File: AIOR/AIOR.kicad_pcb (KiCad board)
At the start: 2 copper layers, 85 x 56.5 mm, 158 parts, among them J20 Conn_01x04, J30 Conn_01x02, J31 Conn_01x02, J50 Conn_01x02, J70 Conn_01x01, J81 Conn_01x06, J82 5V 12V, J90 Conn_01x03, P1 CONN_02X20, P2 CONN_01X02, P3 CAN, P50 XPN, P60 SLX, P70 LCN, P8 Conn_01x02, P9 Conn_01x04, Q30 BTN8982TA, Q31 BTN8982TA, Q60 BC817, Q70 BC817, Q90 BC857, Q91 BC857, U1 MCP2517FD, U2 ISO1050, U20 L7833, U21 L7805, U22 DSPIC33EP128GM604, U23 Si8605, U24 MCP2562, U4 P82B715, U40 C8051F502, U41 ADUM1251, U42 MCP2561, U50 MAX3072E, U70 LM393, U81 L7805, U82 SI8641-SOIC, U83 4504, U90 SAA6579, Y1 4MHz, Y20 8MHz, Y90 4MHz

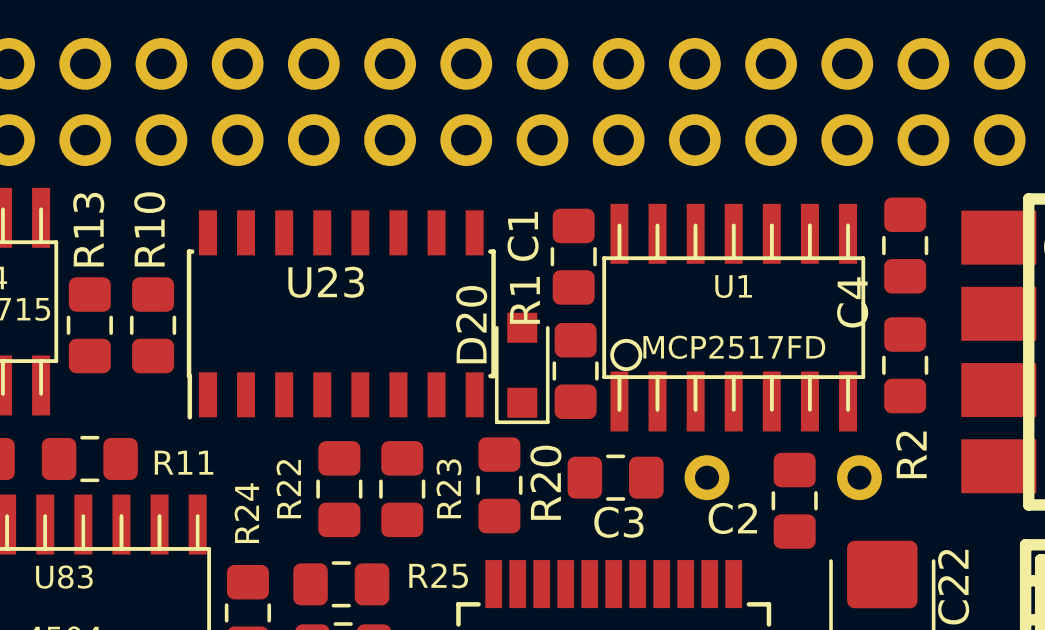
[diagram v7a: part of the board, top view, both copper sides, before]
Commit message: change some footprints
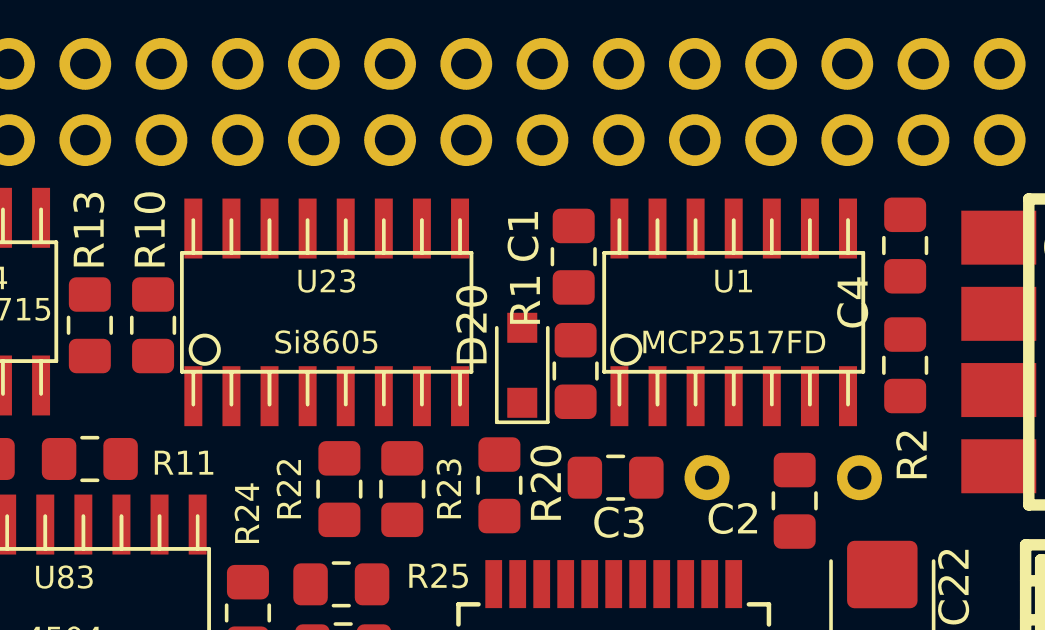
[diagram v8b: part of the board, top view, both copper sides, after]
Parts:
- U23: footprint Package_SO:SOIC-16_3.9x9.9mm_P1.27mm -> w_smd_dil:so-16
- moved U23 0.49 mm to (149.5, 82.5), turned to 0 degrees
- moved U1 0.18 mm to (163.1, 82.5)
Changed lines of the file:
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@@
-(kicad_pcb (version 20171130) (host pcbnew 5.1.2-f72e74a~84~ubuntu18.04.1)
+(kicad_pcb (version 20171130) (host pcbnew "(5.1.2-1)-1")
   (general
     (thickness 1.6)
@@
     (add_net "Net-(U1-Pad3)")
   )
+  (module w_smd_dil:so-16 (layer F.Cu)
+    (at 149.5 82.5)
+    (descr SO-16)
+    (fp_text reference U23 (at 0 -1.016) (layer F.SilkS)
+      (effects (font (size 0.7493 0.7493) (thickness 0.14986)))
+    )
+    (fp_text value Si8605 (at 0 1.016) (layer F.SilkS)
+      (effects (font (size 0.7493 0.7493) (thickness 0.14986)))
+    )
+    (fp_line (start 4.826 -1.9812) (end -4.826 -1.9812) (layer F.SilkS) (width 0.127))
+    (fp_line (start 4.826 1.9812) (end 4.826 -1.9812) (layer F.SilkS) (width 0.127))
+    (fp_line (start -4.826 1.9812) (end 4.826 1.9812) (layer F.SilkS) (width 0.127))
+    (fp_line (start -4.826 -1.9812) (end -4.826 1.9812) (layer F.SilkS) (width 0.127))
+    (fp_circle (center -4.064 1.2446) (end -4.3434 1.6256) (layer F.SilkS) (width 0.127))
+    (fp_line (start -1.905 3.0734) (end -1.905 1.9812) (layer F.SilkS) (width 0.127))
+    (fp_line (start -0.635 3.0734) (end -0.635 1.9812) (layer F.SilkS) (width 0.127))
+    (fp_line (start 0.635 3.0734) (end 0.635 1.9812) (layer F.SilkS) (width 0.127))
+    (fp_line (start -3.175 3.0734) (end -3.175 1.9812) (layer F.SilkS) (width 0.127))
+    (fp_line (start -4.445 1.9812) (end -4.445 3.0734) (layer F.SilkS) (width 0.127))
+    (fp_line (start 1.905 1.9812) (end 1.905 3.0734) (layer F.SilkS) (width 0.127))
+    (fp_line (start 3.175 1.9812) (end 3.175 3.0734) (layer F.SilkS) (width 0.127))
+    (fp_line (start 4.445 1.9812) (end 4.445 3.0734) (layer F.SilkS) (width 0.127))
+    (fp_line (start 4.445 -3.0734) (end 4.445 -1.9812) (layer F.SilkS) (width 0.127))
+    (fp_line (start 3.175 -3.0734) (end 3.175 -1.9812) (layer F.SilkS) (width 0.127))
+    (fp_line (start 1.905 -3.0734) (end 1.905 -1.9812) (layer F.SilkS) (width 0.127))
+    (fp_line (start -4.445 -3.0734) (end -4.445 -1.9812) (layer F.SilkS) (width 0.127))
+    (fp_line (start -3.175 -1.9812) (end -3.175 -3.0734) (layer F.SilkS) (width 0.127))
+    (fp_line (start 0.635 -1.9812) (end 0.635 -3.0734) (layer F.SilkS) (width 0.127))
+    (fp_line (start -0.635 -1.9812) (end -0.635 -3.0734) (layer F.SilkS) (width 0.127))
+    (fp_line (start -1.905 -1.9812) (end -1.905 -3.0734) (layer F.SilkS) (width 0.127))
+    (pad 16 smd rect (at -4.445 -2.794) (size 0.59944 1.99898) (layers F.Cu F.Paste F.Mask)
+      (net 3 +3V3))
+    (pad 15 smd rect (at -3.175 -2.794) (size 0.59944 1.99898) (layers F.Cu F.Paste F.Mask)
+      (net 153 "Net-(U23-Pad15)"))
+    (pad 14 smd rect (at -1.905 -2.794) (size 0.59944 1.99898) (layers F.Cu F.Paste F.Mask)
+      (net 29 /GPIO4))
+    (pad 13 smd rect (at -0.635 -2.794) (size 0.59944 1.99898) (layers F.Cu F.Paste F.Mask)
+      (net 32 /GPIO17))
+    (pad 12 smd rect (at 0.635 -2.794) (size 0.59944 1.99898) (layers F.Cu F.Paste F.Mask)
+      (net 30 /TxD))
+    (pad 11 smd rect (at 1.905 -2.794) (size 0.59944 1.99898) (layers F.Cu F.Paste F.Mask)
+      (net 31 /RxD))
+    (pad 10 smd rect (at 3.175 -2.794) (size 0.59944 1.99898) (layers F.Cu F.Paste F.Mask)
+      (net 152 "Net-(U23-Pad10)"))
+    (pad 9 smd rect (at 4.445 -2.794) (size 0.59944 1.99898) (layers F.Cu F.Paste F.Mask)
+      (net 1 GND))
+    (pad 8 smd rect (at 4.445 2.794) (size 0.59944 1.99898) (layers F.Cu F.Paste F.Mask)
+      (net 42 GNDA))
+    (pad 7 smd rect (at 3.175 2.794) (size 0.59944 1.99898) (layers F.Cu F.Paste F.Mask)
+      (net 151 "Net-(U23-Pad7)"))
+    (pad 6 smd rect (at 1.905 2.794) (size 0.59944 1.99898) (layers F.Cu F.Paste F.Mask)
+      (net 107 /PGD))
+    (pad 5 smd rect (at 0.635 2.794) (size 0.59944 1.99898) (layers F.Cu F.Paste F.Mask)
+      (net 106 /PGC))
+    (pad 4 smd rect (at -0.635 2.794) (size 0.59944 1.99898) (layers F.Cu F.Paste F.Mask)
+      (net 143 /XINT))
+    (pad 3 smd rect (at -1.905 2.794) (size 0.59944 1.99898) (layers F.Cu F.Paste F.Mask)
+      (net 70 /MCLR))
+    (pad 2 smd rect (at -3.175 2.794) (size 0.59944 1.99898) (layers F.Cu F.Paste F.Mask)
+      (net 150 "Net-(U23-Pad2)"))
+    (pad 1 smd rect (at -4.445 2.794) (size 0.59944 1.99898) (layers F.Cu F.Paste F.Mask)
+      (net 3 +3V3))
+    (model walter/smd_dil/so-16.wrl
+      (at (xyz 0 0 0))
+      (scale (xyz 1 1 1))
+      (rotate (xyz 0 0 0))
+    )
+  )
   (module Connector_PinHeader_1.27mm:PinHeader_1x04_P1.27mm_Vertical (layer F.Cu)
     (at 161.29 105.918 90)
@@
   )
   (module w_smd_dil:so-14 (layer F.Cu)
-    (at 163.068 82.677)
+    (at 163.068 82.5)
     (descr SO-14)
     (fp_text reference U1 (at 0 -1.016) (layer F.SilkS)
@@
       (at (xyz 0 0 0))
       (scale (xyz 1 1 1))
-      (rotate (xyz 0 0 0))
-    )
-  )
-  (module Package_SO:SOIC-16_3.9x9.9mm_P1.27mm (layer F.Cu)
-    (at 149.987 82.55 90)
-    (descr "16-Lead Plastic Small Outline (SL) - Narrow, 3.90 mm Body [SOIC] (see Microchip Packaging Specification 00000049BS.pdf)")
-    (tags "SOIC 1.27")
-    (attr smd)
-    (fp_text reference U23 (at 1.016 -0.508 180) (layer F.SilkS)
-      (effects (font (size 1 1) (thickness 0.15)))
-    )
-    (fp_text value Si8605 (at -1.016 0.254) (layer F.Fab)
-      (effects (font (size 1 1) (thickness 0.15)))
-    )
-    (fp_text user %R (at 1.016 -0.254 180) (layer F.Fab)
-      (effects (font (size 0.9 0.9) (thickness 0.135)))
-    )
-    (fp_line (start -0.95 -4.95) (end 1.95 -4.95) (layer F.Fab) (width 0.15))
-    (fp_line (start 1.95 -4.95) (end 1.95 4.95) (layer F.Fab) (width 0.15))
-    (fp_line (start 1.95 4.95) (end -1.95 4.95) (layer F.Fab) (width 0.15))
-    (fp_line (start -1.95 4.95) (end -1.95 -3.95) (layer F.Fab) (width 0.15))
-    (fp_line (start -1.95 -3.95) (end -0.95 -4.95) (layer F.Fab) (width 0.15))
-    (fp_line (start -3.7 -5.25) (end -3.7 5.25) (layer F.CrtYd) (width 0.05))
-    (fp_line (start 3.7 -5.25) (end 3.7 5.25) (layer F.CrtYd) (width 0.05))
-    (fp_line (start -3.7 -5.25) (end 3.7 -5.25) (layer F.CrtYd) (width 0.05))
-    (fp_line (start -3.7 5.25) (end 3.7 5.25) (layer F.CrtYd) (width 0.05))
-    (fp_line (start -2.075 -5.075) (end -2.075 -5.05) (layer F.SilkS) (width 0.15))
-    (fp_line (start 2.075 -5.075) (end 2.075 -4.97) (layer F.SilkS) (width 0.15))
-    (fp_line (start 2.075 5.075) (end 2.075 4.97) (layer F.SilkS) (width 0.15))
-    (fp_line (start -2.075 5.075) (end -2.075 4.97) (layer F.SilkS) (width 0.15))
-    (fp_line (start -2.075 -5.075) (end 2.075 -5.075) (layer F.SilkS) (width 0.15))
-    (fp_line (start -2.075 5.075) (end 2.075 5.075) (layer F.SilkS) (width 0.15))
-    (fp_line (start -2.075 -5.05) (end -3.45 -5.05) (layer F.SilkS) (width 0.15))
-    (pad 1 smd rect (at -2.7 -4.445 90) (size 1.5 0.6) (layers F.Cu F.Paste F.Mask)
-      (net 3 +3V3))
-    (pad 2 smd rect (at -2.7 -3.175 90) (size 1.5 0.6) (layers F.Cu F.Paste F.Mask)
-      (net 150 "Net-(U23-Pad2)"))
-    (pad 3 smd rect (at -2.7 -1.905 90) (size 1.5 0.6) (layers F.Cu F.Paste F.Mask)
-      (net 70 /MCLR))
-    (pad 4 smd rect (at -2.7 -0.635 90) (size 1.5 0.6) (layers F.Cu F.Paste F.Mask)
-      (net 143 /XINT))
-    (pad 5 smd rect (at -2.7 0.635 90) (size 1.5 0.6) (layers F.Cu F.Paste F.Mask)
-      (net 106 /PGC))
-    (pad 6 smd rect (at -2.7 1.905 90) (size 1.5 0.6) (layers F.Cu F.Paste F.Mask)
-      (net 107 /PGD))
-    (pad 7 smd rect (at -2.7 3.175 90) (size 1.5 0.6) (layers F.Cu F.Paste F.Mask)
-      (net 151 "Net-(U23-Pad7)"))
-    (pad 8 smd rect (at -2.7 4.445 90) (size 1.5 0.6) (layers F.Cu F.Paste F.Mask)
-      (net 42 GNDA))
-    (pad 9 smd rect (at 2.7 4.445 90) (size 1.5 0.6) (layers F.Cu F.Paste F.Mask)
-      (net 1 GND))
-    (pad 10 smd rect (at 2.7 3.175 90) (size 1.5 0.6) (layers F.Cu F.Paste F.Mask)
-      (net 152 "Net-(U23-Pad10)"))
-    (pad 11 smd rect (at 2.7 1.905 90) (size 1.5 0.6) (layers F.Cu F.Paste F.Mask)
-      (net 31 /RxD))
-    (pad 12 smd rect (at 2.7 0.635 90) (size 1.5 0.6) (layers F.Cu F.Paste F.Mask)
-      (net 30 /TxD))
-    (pad 13 smd rect (at 2.7 -0.635 90) (size 1.5 0.6) (layers F.Cu F.Paste F.Mask)
-      (net 32 /GPIO17))
-    (pad 14 smd rect (at 2.7 -1.905 90) (size 1.5 0.6) (layers F.Cu F.Paste F.Mask)
-      (net 29 /GPIO4))
-    (pad 15 smd rect (at 2.7 -3.175 90) (size 1.5 0.6) (layers F.Cu F.Paste F.Mask)
-      (net 153 "Net-(U23-Pad15)"))
-    (pad 16 smd rect (at 2.7 -4.445 90) (size 1.5 0.6) (layers F.Cu F.Paste F.Mask)
-      (net 3 +3V3))
-    (model ${KISYS3DMOD}/Package_SO.3dshapes/SOIC-16_3.9x9.9mm_P1.27mm.wrl
-      (at (xyz 0 0 0))
-      (scale (xyz 1 1 1))
